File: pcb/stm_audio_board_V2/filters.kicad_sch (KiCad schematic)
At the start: 48 parts

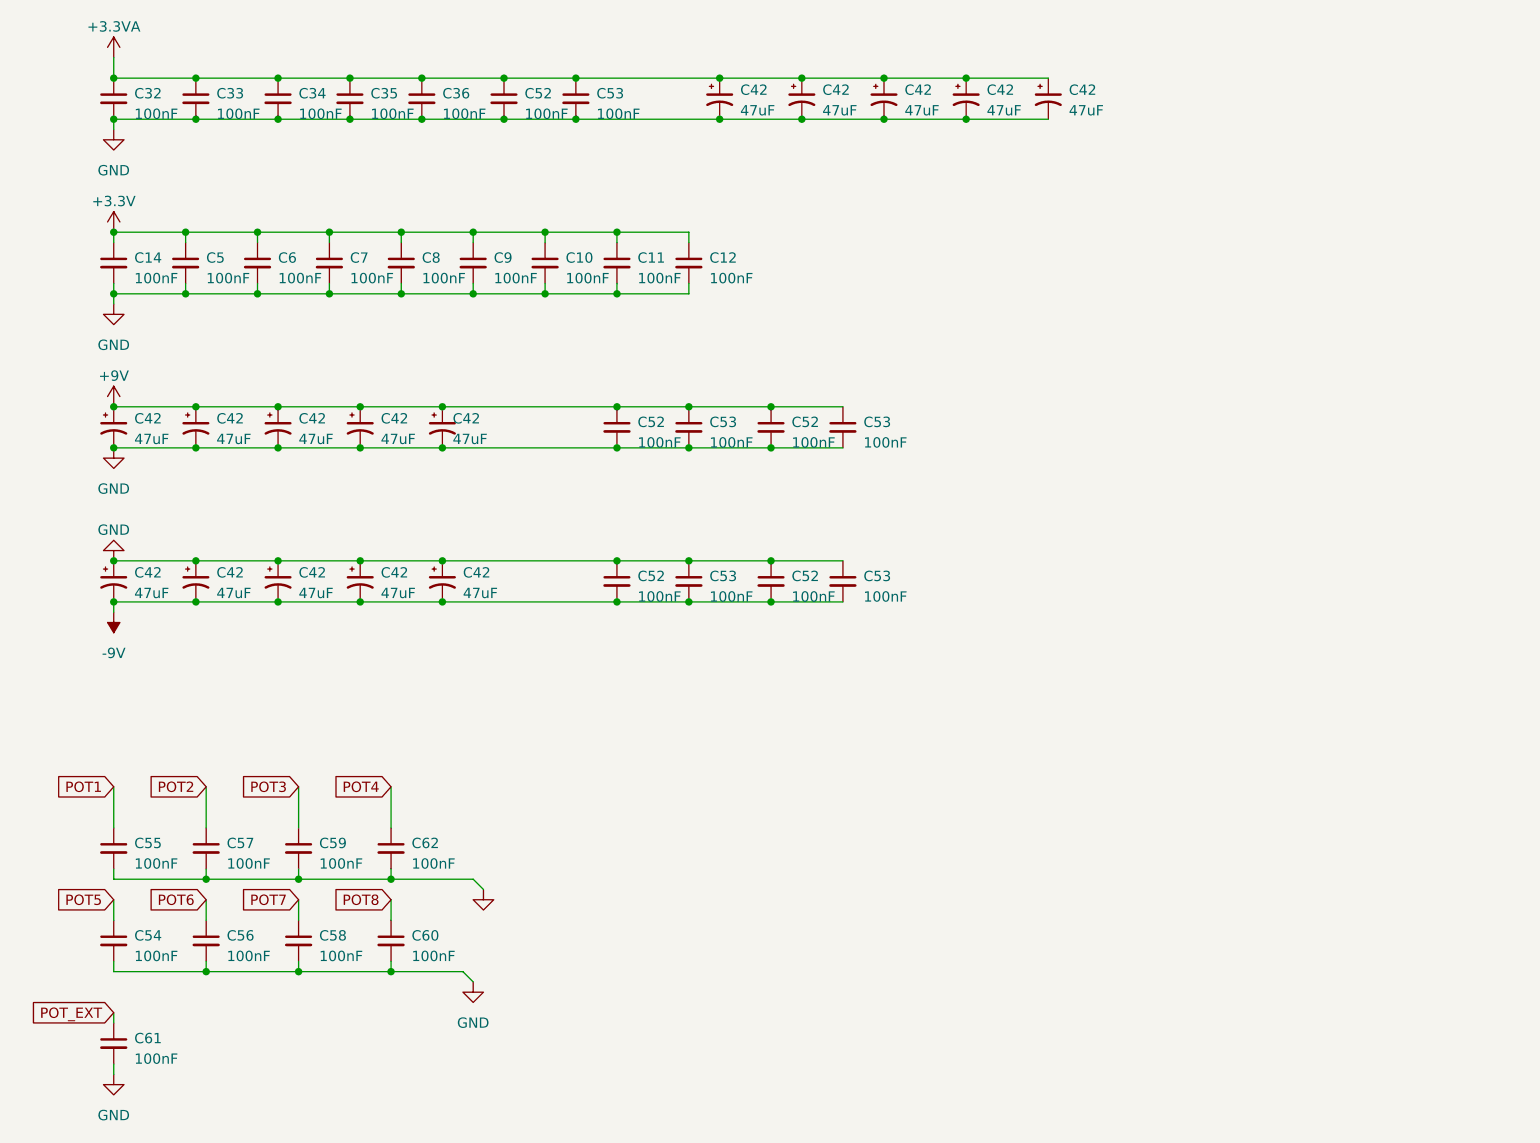
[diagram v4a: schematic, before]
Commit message: Capacitor types are choosen, schematic updated, unused capacitors deleted. Connectors need to be connected to the mcu and its finished
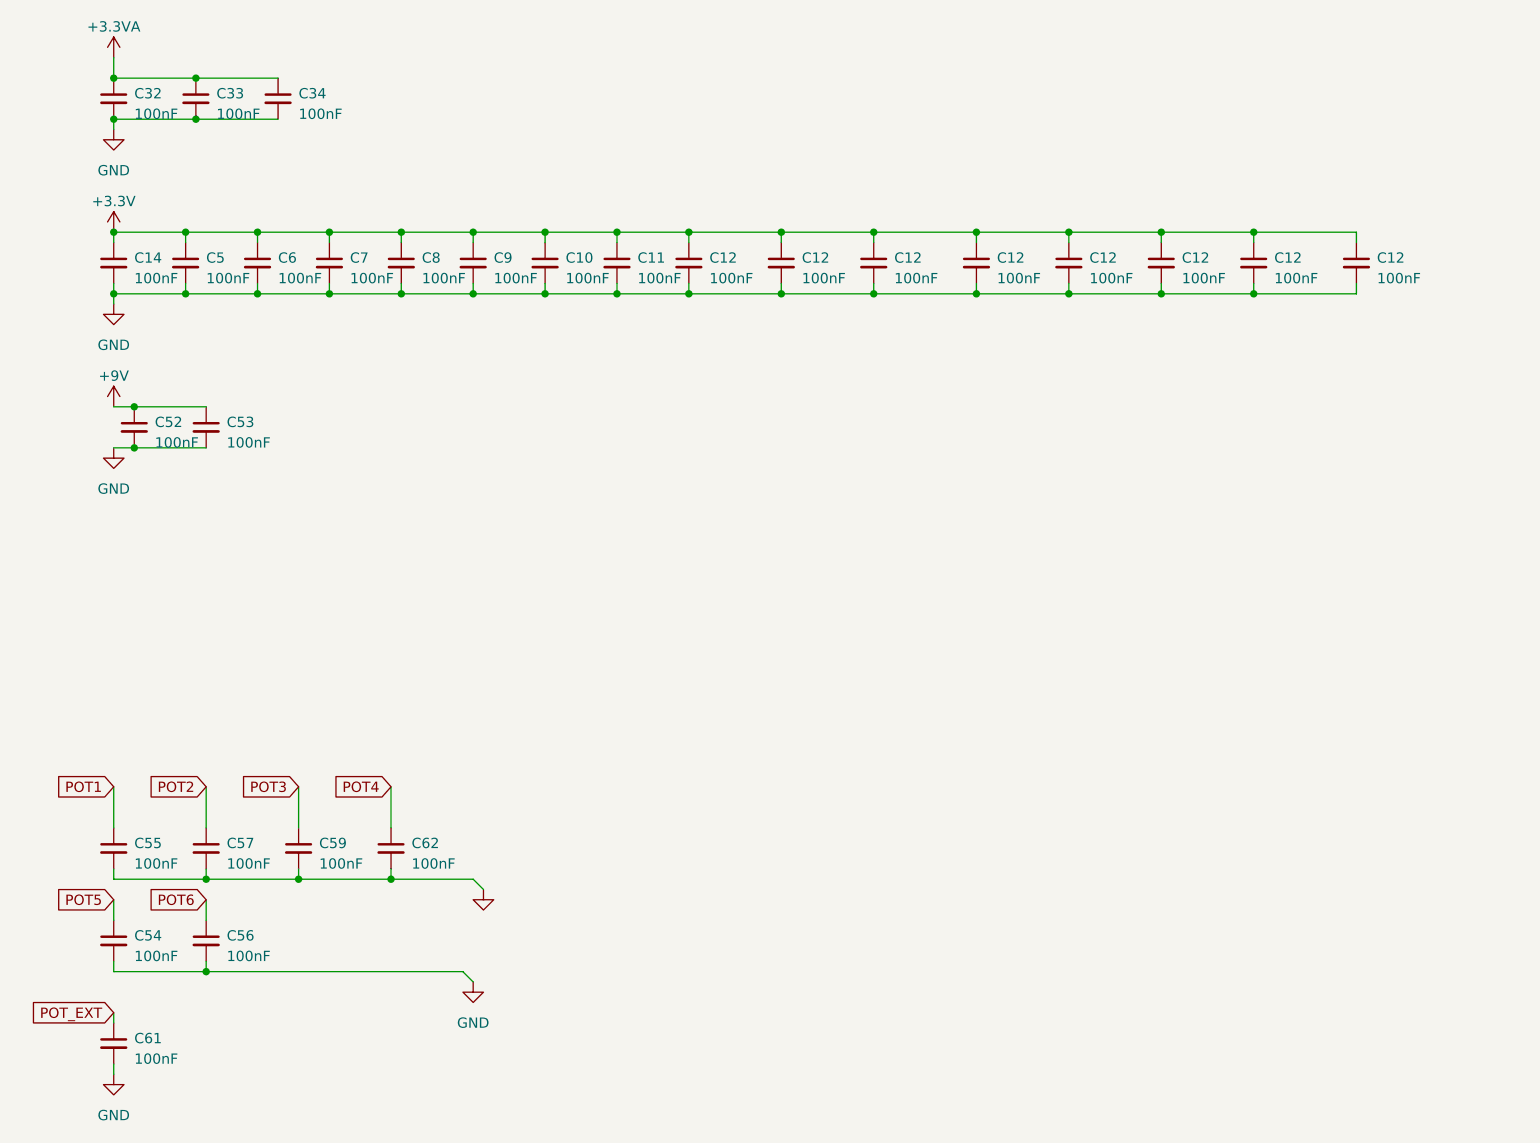
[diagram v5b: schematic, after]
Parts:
- removed C35, C36, C52 (x4), C53 (x4), C58, C60: 100nF, Capacitor_SMD:C_0603_1608Metric_Pad1.08x0.95mm_HandSolder, symbol Device:C_Small
- removed C42 (x15): 47uF, Capacitor_SMD:C_0805_2012Metric_Pad1.18x1.45mm_HandSolder, symbol Device:C_Polarized_Small_US
- added C12 (x7): 100nF, Capacitor_SMD:C_0603_1608Metric_Pad1.08x0.95mm_HandSolder, symbol Device:C_Small
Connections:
- net +3.3V: now also C12.1, C12.1, C12.1, C12.1, C12.1, C12.1, C12.1
- net GND: now also C12.2, C12.2, C12.2, C12.2, C12.2, C12.2, C12.2
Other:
- moved on the sheet: C52, C53

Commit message: Update stm_audio_board_V2-B_Cu.gbr, stm_audio_board_V2-B_Mask.gbr, and 29 more files...
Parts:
- added C12: 100nF, Capacitor_SMD:C_0603_1608Metric_Pad1.08x0.95mm_HandSolder, symbol Device:C_Small
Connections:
- net +3.3V: now also C12.1
- net GND: now also C12.2
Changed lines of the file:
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@@
   (junction (at 26.67 33.02) (diameter 0) (color 0 0 0 0)
   )
+  (junction (at 180.34 54.61) (diameter 0) (color 0 0 0 0)
+  )
   (junction (at 49.53 127) (diameter 0) (color 0 0 0 0)
   )
@@
   (junction (at 29.21 73.66) (diameter 0) (color 0 0 0 0)
   )
+  (junction (at 180.34 46.99) (diameter 0) (color 0 0 0 0)
+  )
   (junction (at 62.23 54.61) (diameter 0) (color 0 0 0 0)
   )
@@
     (stroke (width 0) (type default))
   )
+  (wire (pts (xy 191.77 48.26) (xy 191.77 46.99))
+    (stroke (width 0) (type default))
+  )
   (wire (pts (xy 38.1 137.16) (xy 38.1 138.43))
     (stroke (width 0) (type default))
@@
     (stroke (width 0) (type default))
   )
+  (wire (pts (xy 191.77 46.99) (xy 180.34 46.99))
+    (stroke (width 0) (type default))
+  )
   (wire (pts (xy 80.01 48.26) (xy 80.01 46.99))
     (stroke (width 0) (type default))
@@
     (stroke (width 0) (type default))
   )
+  (wire (pts (xy 180.34 54.61) (xy 191.77 54.61))
+    (stroke (width 0) (type default))
+  )
   (wire (pts (xy 44.45 46.99) (xy 53.34 46.99))
     (stroke (width 0) (type default))
@@
   )
   (wire (pts (xy 88.9 53.34) (xy 88.9 54.61))
+    (stroke (width 0) (type default))
+  )
+  (wire (pts (xy 191.77 53.34) (xy 191.77 54.61))
     (stroke (width 0) (type default))
   )
@@
         )
       )
+    )
+  )
+  (symbol (lib_id "Device:C_Small") (at 191.77 50.8 0) (unit 1)
+    (in_bom yes) (on_board yes) (dnp no)
+    (property "Reference" "C12" (at 194.31 50.1713 0)
+      (effects (font (size 1.27 1.27)) (justify left))
+    )
+    (property "Value" "100nF" (at 194.31 52.7113 0)
+      (effects (font (size 1.27 1.27)) (justify left))
+    )
+    (property "Footprint" "Capacitor_SMD:C_0603_1608Metric_Pad1.08x0.95mm_HandSolder" (at 191.77 50.8 0)
+      (effects (font (size 1.27 1.27)) hide)
+    )
+    (property "Datasheet" "~" (at 191.77 50.8 0)
+      (effects (font (size 1.27 1.27)) hide)
+    )
+    (pin "1")
+    (pin "2")
+    (instances
+      (project "stm_audio_board_V2"
+        (path "/6997cf63-2615-4e49-9471-e7da1b6bae71"
+          (reference "C12") (unit 1)
+        )
+        (path "/6997cf63-2615-4e49-9471-e7da1b6bae71/927539c8-c0d0-4950-9b67-385a1cdd80f8"
+          (reference "C36") (unit 1)
+        )
+      )
